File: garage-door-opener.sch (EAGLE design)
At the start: 17 parts, among them IC1 LM2575-3.3T, K1 RR1A, T1 BC547, X2 Connector

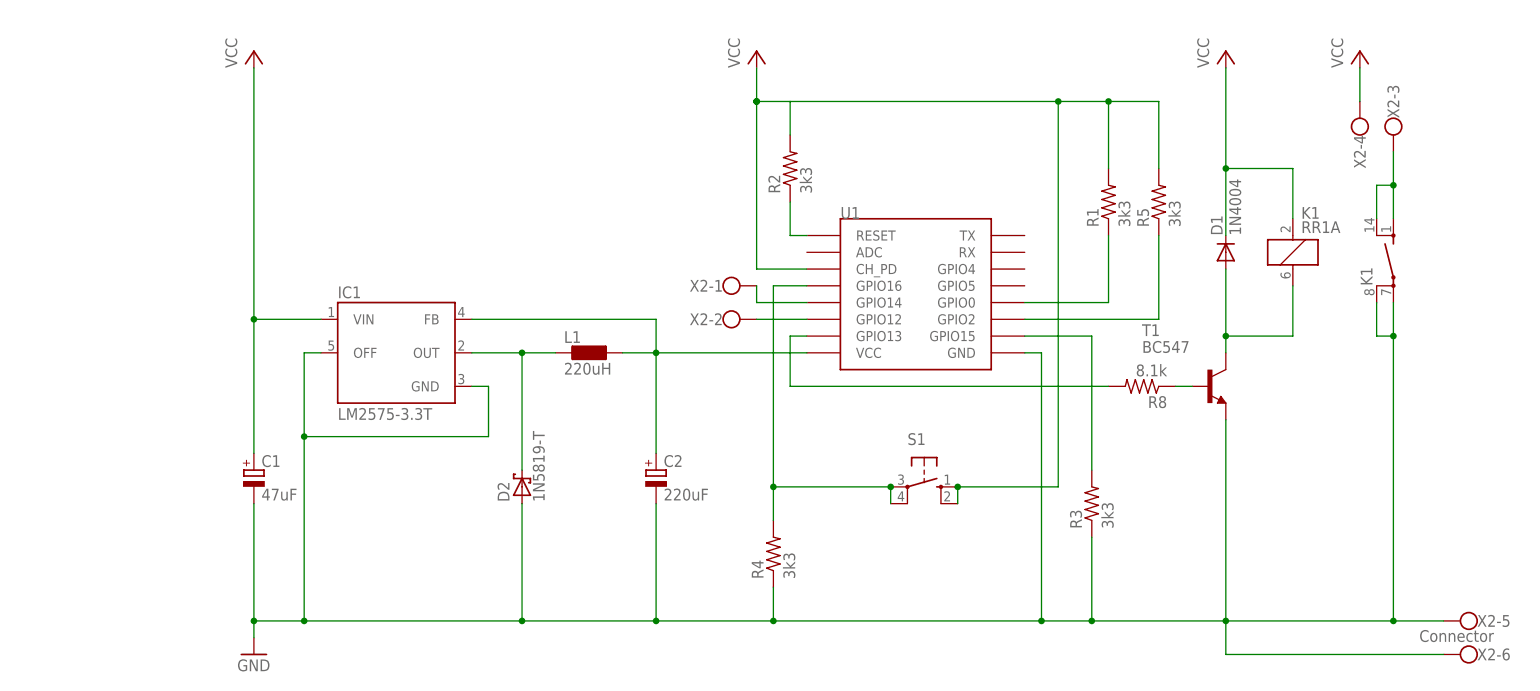
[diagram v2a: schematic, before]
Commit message: Fixing missing node on the VCC net, 12V in was incorrectly linked to VCC. Moved to VIN
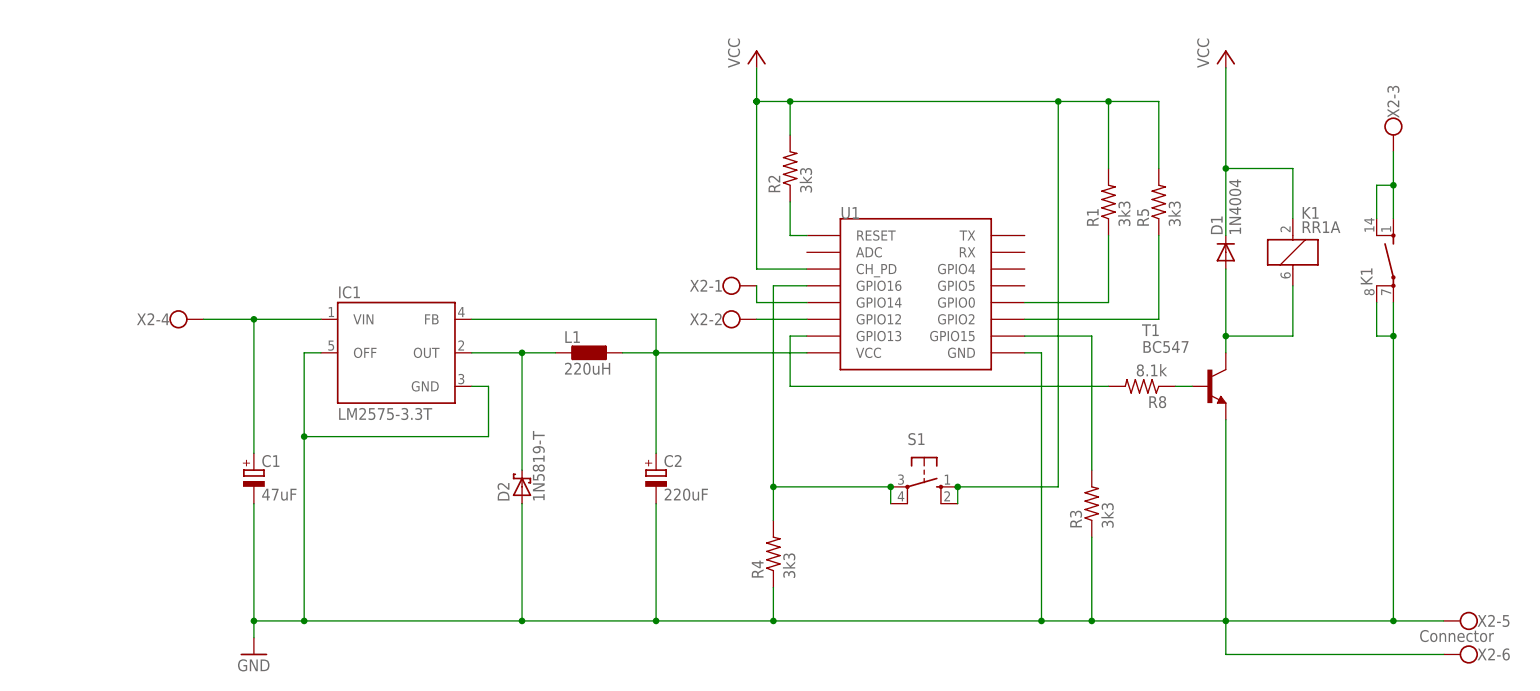
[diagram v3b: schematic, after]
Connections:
- new net VIN: C1.+, IC1.VIN, X2-4.KL
- net VCC: no longer C1.+, IC1.VIN, X2-4.KL
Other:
- moved on the sheet: X2-4
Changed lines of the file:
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@@
 <part name="R8" library="resistor" library_urn="urn:adsk.eagle:library:348" deviceset="R-US_" device="0207/10" package3d_urn="urn:adsk.eagle:package:25939/1" value="8.1k"/>
 <part name="GND2" library="supply1" deviceset="GND" device=""/>
-<part name="P+2" library="supply1" deviceset="VCC" device=""/>
-<part name="P+3" library="supply1" deviceset="VCC" device=""/>
 <part name="U1" library="esp8266modules" deviceset="ESP12" device="SMD"/>
 <part name="IC1" library="lm2575" deviceset="LM2575-3.3" device="T" value="LM2575-3.3T"/>
@@
 <instance part="R8" gate="G$1" x="139.7" y="40.64" rot="R180"/>
 <instance part="GND2" gate="1" x="5.08" y="0"/>
-<instance part="P+2" gate="VCC" x="5.08" y="91.44"/>
-<instance part="P+3" gate="VCC" x="172.72" y="91.44"/>
 <instance part="U1" gate="G$1" x="106.68" y="55.88"/>
 <instance part="IC1" gate="A" x="25.4" y="45.72"/>
@@
 <instance part="X2" gate="-2" x="76.2" y="50.8"/>
 <instance part="X2" gate="-3" x="177.8" y="81.28" rot="R270"/>
-<instance part="X2" gate="-4" x="172.72" y="78.74" smashed="yes" rot="R90">
-<attribute name="NAME" x="171.831" y="78.74" size="1.778" layer="95" rot="R270"/>
+<instance part="X2" gate="-4" x="-7.62" y="50.8" smashed="yes">
+<attribute name="NAME" x="-7.62" y="51.689" size="1.778" layer="95" rot="R180"/>
 </instance>
 <instance part="X2" gate="-5" x="190.5" y="5.08" rot="R180"/>
@@
 </segment>
 <segment>
-<pinref part="P+2" gate="VCC" pin="VCC"/>
-<wire x1="5.08" y1="88.9" x2="5.08" y2="50.8" width="0.1524" layer="91"/>
-<pinref part="IC1" gate="A" pin="VIN"/>
-<wire x1="15.24" y1="50.8" x2="5.08" y2="50.8" width="0.1524" layer="91"/>
-<pinref part="C1" gate="G$1" pin="+"/>
-<wire x1="5.08" y1="30.48" x2="5.08" y2="50.8" width="0.1524" layer="91"/>
-<junction x="5.08" y="50.8"/>
-</segment>
-<segment>
-<pinref part="P+3" gate="VCC" pin="VCC"/>
-<pinref part="X2" gate="-4" pin="KL"/>
-<wire x1="172.72" y1="88.9" x2="172.72" y2="83.82" width="0.1524" layer="91"/>
-</segment>
-<segment>
-<pinref part="R2" gate="G$1" pin="2"/>
-<wire x1="86.36" y1="78.74" x2="86.36" y2="83.82" width="0.1524" layer="91"/>
 <pinref part="R1" gate="G$1" pin="2"/>
 <wire x1="81.28" y1="83.82" x2="86.36" y2="83.82" width="0.1524" layer="91"/>
@@
 <wire x1="142.24" y1="83.82" x2="134.62" y2="83.82" width="0.1524" layer="91"/>
 <junction x="134.62" y="83.82"/>
+<pinref part="R2" gate="G$1" pin="2"/>
+<wire x1="86.36" y1="78.74" x2="86.36" y2="83.82" width="0.1524" layer="91"/>
+<junction x="86.36" y="83.82"/>
 </segment>
 </net>
@@
 </segment>
 </net>
+<net name="VIN" class="0">
+<segment>
+<pinref part="IC1" gate="A" pin="VIN"/>
+<wire x1="15.24" y1="50.8" x2="5.08" y2="50.8" width="0.1524" layer="91"/>
+<pinref part="C1" gate="G$1" pin="+"/>
+<wire x1="5.08" y1="30.48" x2="5.08" y2="50.8" width="0.1524" layer="91"/>
+<pinref part="X2" gate="-4" pin="KL"/>
+<wire x1="-2.54" y1="50.8" x2="5.08" y2="50.8" width="0.1524" layer="91"/>
+<junction x="5.08" y="50.8"/>
+</segment>
+</net>

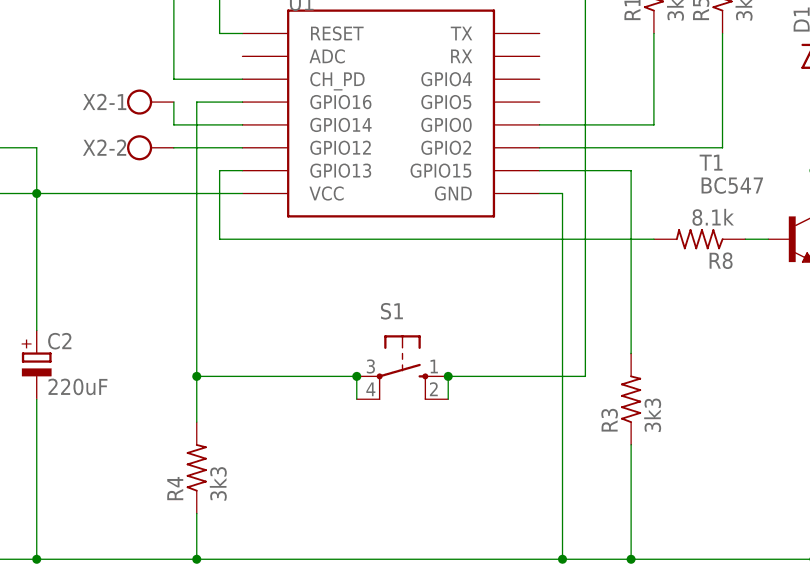
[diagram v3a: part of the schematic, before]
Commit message: Adding pogo pins to ESP8266 for prgoramming. Fixing DRC errors - still some errors with the programmer mount screws.
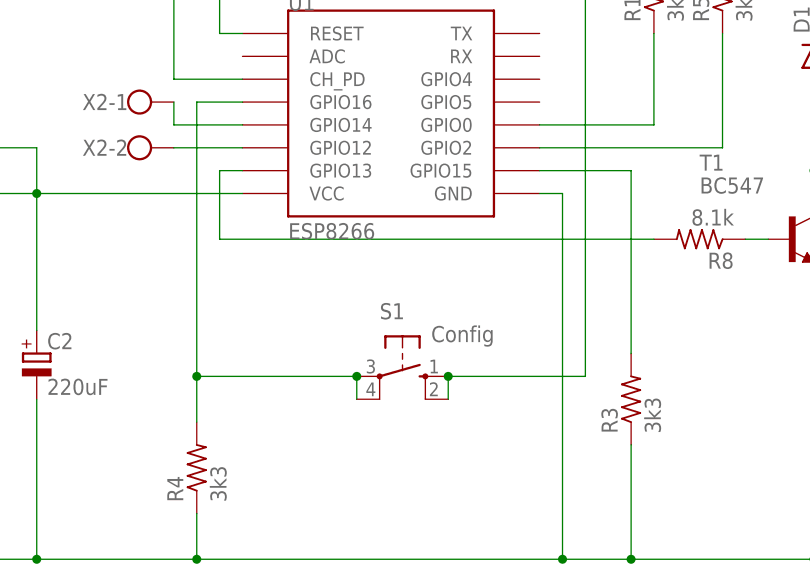
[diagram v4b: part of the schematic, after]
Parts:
- R1, R2, R3, R4, R5, R8: device resistor:R-US_0207/10 -> resistor:R-US_0204/7
- S1: value (none) -> Config
- U1: value (none) -> ESP8266; device esp8266modules:ESP12SMD -> esp8266modules:ESP12ESP12-SMD-POGO
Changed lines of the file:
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@@
 <?xml version="1.0" encoding="utf-8"?>
 <!DOCTYPE eagle SYSTEM "eagle.dtd">
-<eagle version="8.6.0">
+<eagle version="8.7.1">
 <drawing>
 <settings>
@@
 <grid distance="0.1" unitdist="inch" unit="inch" style="lines" multiple="1" display="no" altdistance="0.01" altunitdist="inch" altunit="inch"/>
 <layers>
-<layer number="1" name="Top" color="4" fill="1" visible="no" active="no"/>
-<layer number="16" name="Bottom" color="1" fill="1" visible="no" active="no"/>
-<layer number="17" name="Pads" color="2" fill="1" visible="no" active="no"/>
-<layer number="18" name="Vias" color="2" fill="1" visible="no" active="no"/>
-<layer number="19" name="Unrouted" color="6" fill="1" visible="no" active="no"/>
-<layer number="20" name="Dimension" color="15" fill="1" visible="no" active="no"/>
-<layer number="21" name="tPlace" color="7" fill="1" visible="no" active="no"/>
-<layer number="22" name="bPlace" color="7" fill="1" visible="no" active="no"/>
-<layer number="23" name="tOrigins" color="15" fill="1" visible="no" active="no"/>
-<layer number="24" name="bOrigins" color="15" fill="1" visible="no" active="no"/>
-<layer number="25" name="tNames" color="7" fill="1" visible="no" active="no"/>
-<layer number="26" name="bNames" color="7" fill="1" visible="no" active="no"/>
-<layer number="27" name="tValues" color="7" fill="1" visible="no" active="no"/>
-<layer number="28" name="bValues" color="7" fill="1" visible="no" active="no"/>
+<layer number="1" name="Top" color="4" fill="1" visible="yes" active="no"/>
+<layer number="16" name="Bottom" color="1" fill="1" visible="yes" active="no"/>
+<layer number="17" name="Pads" color="2" fill="1" visible="yes" active="no"/>
+<layer number="18" name="Vias" color="2" fill="1" visible="yes" active="no"/>
+<layer number="19" name="Unrouted" color="6" fill="1" visible="yes" active="no"/>
+<layer number="20" name="Dimension" color="15" fill="1" visible="yes" active="no"/>
+<layer number="21" name="tPlace" color="7" fill="1" visible="yes" active="no"/>
+<layer number="22" name="bPlace" color="7" fill="1" visible="yes" active="no"/>
+<layer number="23" name="tOrigins" color="15" fill="1" visible="yes" active="no"/>
+<layer number="24" name="bOrigins" color="15" fill="1" visible="yes" active="no"/>
+<layer number="25" name="tNames" color="7" fill="1" visible="yes" active="no"/>
+<layer number="26" name="bNames" color="7" fill="1" visible="yes" active="no"/>
+<layer number="27" name="tValues" color="7" fill="1" visible="yes" active="no"/>
+<layer number="28" name="bValues" color="7" fill="1" visible="yes" active="no"/>
 <layer number="29" name="tStop" color="7" fill="3" visible="no" active="no"/>
 <layer number="30" name="bStop" color="7" fill="6" visible="no" active="no"/>
@@
 <layer number="35" name="tGlue" color="7" fill="4" visible="no" active="no"/>
 <layer number="36" name="bGlue" color="7" fill="5" visible="no" active="no"/>
-<layer number="37" name="tTest" color="7" fill="1" visible="no" active="no"/>
-<layer number="38" name="bTest" color="7" fill="1" visible="no" active="no"/>
+<layer number="37" name="tTest" color="7" fill="1" visible="yes" active="no"/>
+<layer number="38" name="bTest" color="7" fill="1" visible="yes" active="no"/>
 <layer number="39" name="tKeepout" color="4" fill="11" visible="no" active="no"/>
 <layer number="40" name="bKeepout" color="1" fill="11" visible="no" active="no"/>
@@
 <layer number="44" name="Drills" color="7" fill="1" visible="no" active="no"/>
 <layer number="45" name="Holes" color="7" fill="1" visible="no" active="no"/>
-<layer number="46" name="Milling" color="3" fill="1" visible="no" active="no"/>
-<layer number="47" name="Measures" color="7" fill="1" visible="no" active="no"/>
-<layer number="48" name="Document" color="7" fill="1" visible="no" active="no"/>
-<layer number="49" name="Reference" color="7" fill="1" visible="no" active="no"/>
-<layer number="50" name="dxf" color="7" fill="1" visible="no" active="no"/>
-<layer number="51" name="tDocu" color="7" fill="1" visible="no" active="no"/>
-<layer number="52" name="bDocu" color="7" fill="1" visible="no" active="no"/>
-<layer number="53" name="tGND_GNDA" color="7" fill="9" visible="no" active="no"/>
-<layer number="54" name="bGND_GNDA" color="1" fill="9" visible="no" active="no"/>
-<layer number="56" name="wert" color="7" fill="1" visible="no" active="no"/>
-<layer number="57" name="tCAD" color="7" fill="1" visible="no" active="no"/>
-<layer number="59" name="tCarbon" color="7" fill="1" visible="no" active="no"/>
-<layer number="60" name="bCarbon" color="7" fill="1" visible="no" active="no"/>
+<layer number="46" name="Milling" color="3" fill="1" visible="yes" active="no"/>
+<layer number="47" name="Measures" color="7" fill="1" visible="yes" active="no"/>
+<layer number="48" name="Document" color="7" fill="1" visible="yes" active="no"/>
+<layer number="49" name="Reference" color="7" fill="1" visible="yes" active="no"/>
+<layer number="50" name="dxf" color="7" fill="1" visible="yes" active="no"/>
+<layer number="51" name="tDocu" color="7" fill="1" visible="yes" active="no"/>
+<layer number="52" name="bDocu" color="7" fill="1" visible="yes" active="no"/>
+<layer number="53" name="tGND_GNDA" color="7" fill="9" visible="yes" active="no"/>
+<layer number="54" name="bGND_GNDA" color="1" fill="9" visible="yes" active="no"/>
+<layer number="56" name="wert" color="7" fill="1" visible="yes" active="no"/>
+<layer number="57" name="tCAD" color="7" fill="1" visible="yes" active="no"/>
+<layer number="59" name="tCarbon" color="7" fill="1" visible="yes" active="no"/>
+<layer number="60" name="bCarbon" color="7" fill="1" visible="yes" active="no"/>
 <layer number="90" name="Modules" color="5" fill="1" visible="yes" active="yes"/>
 <layer number="91" name="Nets" color="2" fill="1" visible="yes" active="yes"/>
@@
 <part name="D1" library="diode" deviceset="1N4004" device=""/>
 <part name="T1" library="transistor" deviceset="BC547" device=""/>
-<part name="R8" library="resistor" library_urn="urn:adsk.eagle:library:348" deviceset="R-US_" device="0207/10" package3d_urn="urn:adsk.eagle:package:25939/1" value="8.1k"/>
+<part name="R8" library="resistor" library_urn="urn:adsk.eagle:library:348" deviceset="R-US_" device="0204/7" package3d_urn="urn:adsk.eagle:package:25945/1" value="8.1k"/>
 <part name="GND2" library="supply1" deviceset="GND" device=""/>
-<part name="U1" library="esp8266modules" deviceset="ESP12" device="SMD"/>
+<part name="U1" library="esp8266modules" deviceset="ESP12" device="ESP12-SMD-POGO" value="ESP8266"/>
 <part name="IC1" library="lm2575" deviceset="LM2575-3.3" device="T" value="LM2575-3.3T"/>
 <part name="C1" library="rcl" library_urn="urn:adsk.eagle:library:334" deviceset="CPOL-EU" device="E5-4" package3d_urn="urn:adsk.eagle:package:23370/1" value="47uF"/>
@@
 <part name="L1" library="eagle-ltspice" library_urn="urn:adsk.eagle:library:217" deviceset="L" device="0207/10" package3d_urn="urn:adsk.eagle:package:13275/1" value="220uH"/>
 <part name="P+4" library="supply1" deviceset="VCC" device=""/>
-<part name="R1" library="resistor" library_urn="urn:adsk.eagle:library:348" deviceset="R-US_" device="0207/10" package3d_urn="urn:adsk.eagle:package:25939/1" value="3k3"/>
-<part name="R2" library="resistor" library_urn="urn:adsk.eagle:library:348" deviceset="R-US_" device="0207/10" package3d_urn="urn:adsk.eagle:package:25939/1" value="3k3"/>
-<part name="R3" library="resistor" library_urn="urn:adsk.eagle:library:348" deviceset="R-US_" device="0207/10" package3d_urn="urn:adsk.eagle:package:25939/1" value="3k3"/>
+<part name="R1" library="resistor" library_urn="urn:adsk.eagle:library:348" deviceset="R-US_" device="0204/7" package3d_urn="urn:adsk.eagle:package:25945/1" value="3k3"/>
+<part name="R2" library="resistor" library_urn="urn:adsk.eagle:library:348" deviceset="R-US_" device="0204/7" package3d_urn="urn:adsk.eagle:package:25945/1" value="3k3"/>
+<part name="R3" library="resistor" library_urn="urn:adsk.eagle:library:348" deviceset="R-US_" device="0204/7" package3d_urn="urn:adsk.eagle:package:25945/1" value="3k3"/>
 <part name="K1" library="relay" library_urn="urn:adsk.eagle:library:339" deviceset="RR1A" device="" package3d_urn="urn:adsk.eagle:package:24316/1"/>
 <part name="X2" library="con-wago-500" library_urn="urn:adsk.eagle:library:195" deviceset="W237-6" device="" package3d_urn="urn:adsk.eagle:package:10696/1" value="Connector"/>
-<part name="S1" library="switch-omron" library_urn="urn:adsk.eagle:library:377" deviceset="10-XX" device="" package3d_urn="urn:adsk.eagle:package:27496/1"/>
-<part name="R4" library="resistor" library_urn="urn:adsk.eagle:library:348" deviceset="R-US_" device="0207/10" package3d_urn="urn:adsk.eagle:package:25939/1" value="3k3"/>
-<part name="R5" library="resistor" library_urn="urn:adsk.eagle:library:348" deviceset="R-US_" device="0207/10" package3d_urn="urn:adsk.eagle:package:25939/1" value="3k3"/>
+<part name="S1" library="switch-omron" library_urn="urn:adsk.eagle:library:377" deviceset="10-XX" device="" package3d_urn="urn:adsk.eagle:package:27496/1" value="Config"/>
+<part name="R4" library="resistor" library_urn="urn:adsk.eagle:library:348" deviceset="R-US_" device="0204/7" package3d_urn="urn:adsk.eagle:package:25945/1" value="3k3"/>
+<part name="R5" library="resistor" library_urn="urn:adsk.eagle:library:348" deviceset="R-US_" device="0204/7" package3d_urn="urn:adsk.eagle:package:25945/1" value="3k3"/>
 </parts>
 <sheets>
